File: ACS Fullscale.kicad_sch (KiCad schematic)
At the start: 19 parts, among them J1 Pulse-20, J2 Conn_01x02, U1 SN65HVD230, U11 R-78E5.0-1.0, U2 MS5611-01BA, U3 4001, U4 Teensy4.1, U5 TPS62202DBV, U6 BHI360, U7 TXS0108EPW

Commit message: hi
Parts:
- removed U3: 4001, symbol 4xxx_IEEE:4001
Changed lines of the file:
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@@
-	(wire
-		(pts
-			(xy 72.39 138.43) (xy 120.65 138.43)
-		)
-		(stroke
-			(width 0)
-			(type default)
-		)
-	)
 	(wire
 		(pts
@@
 	(wire
 		(pts
-			(xy 139.7 143.51) (xy 139.7 127)
-		)
-		(stroke
-			(width 0)
-			(type default)
-		)
-	)
-	(wire
-		(pts
 			(xy 38.1 31.75) (xy 38.1 48.26)
 		)
@@
 	(wire
 		(pts
-			(xy 156.21 154.94) (xy 156.21 162.56)
-		)
-		(stroke
-			(width 0)
-			(type default)
-		)
-	)
-	(wire
-		(pts
 			(xy 73.66 109.22) (xy 81.28 109.22)
 		)
@@
 	(wire
 		(pts
-			(xy 163.83 162.56) (xy 156.21 162.56)
-		)
-		(stroke
-			(width 0)
-			(type default)
-		)
-	)
-	(wire
-		(pts
 			(xy 95.25 31.75) (xy 95.25 33.02)
 		)
@@
 		(pts
 			(xy 80.01 165.1) (xy 80.01 167.64)
-		)
-		(stroke
-			(width 0)
-			(type default)
-		)
-	)
-	(wire
-		(pts
-			(xy 127 127) (xy 139.7 127)
 		)
 		(stroke
@@
 					(unit 1)
 				)
-			)
-		)
-	)
-	(symbol
-		(lib_id "4xxx_IEEE:4001")
-		(at 81.28 144.78 0)
-		(unit 1)
-		(exclude_from_sim no)
-		(in_bom yes)
-		(on_board yes)
-		(dnp no)
-		(fields_autoplaced yes)
-		(property "Reference" "U3"
-			(at 90.17 138.3598 0)
-			(effects
-				(font
-					(size 1.27 1.27)
-				)
-			)
-		)
-		(property "Value" "4001"
-			(at 90.17 140.8998 0)
-			(effects
-				(font
-					(size 1.27 1.27)
-				)
-			)
-		)
-		(property "Footprint" ""
-			(at 81.28 144.78 0)
-			(effects
-				(font
-					(size 1.27 1.27)
-				)
-				(hide yes)
-			)
-		)
-		(property "Datasheet" ""
-			(at 81.28 144.78 0)
-			(effects
-				(font
-					(size 1.27 1.27)
-				)
-				(hide yes)
-			)
-		)
-		(property "Description" ""
-			(at 81.28 144.78 0)
-			(effects
-				(font
-					(size 1.27 1.27)
-				)
-				(hide yes)
-			)
-		)
-		(pin "9"
-		)
-		(pin "12"
-		)
-		(pin "10"
-		)
-		(pin "13"
-		)
-		(pin "11"
-		)
-		(pin "8"
-		)
-		(pin "4"
-		)
-		(pin "6"
-		)
-		(pin "5"
-		)
-		(pin "3"
-		)
-		(pin "2"
-		)
-		(pin "1"
-		)
-		(pin "7"
-		)
-		(pin "14"
-		)
-		(instances
-			(project ""
-				(path "/51f244b9-9601-4f29-b08e-b866e02fd2b7"
-					(reference "U3")
-					(unit 1)
-				)

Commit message: fix lib
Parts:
- removed J1: Pulse-20, Sensor_Motion:Pulse-20, symbol Sensor_Motion:Pulse-20
- removed U11: R-78E5.0-1.0, R-78E5.0-1.0:R-78C&slash_E-1.0_SIP3_11.6X8.5X10.4_RCP, symbol R-78E5.0-1.0:R-78E5.0-1.0
- removed U4: Teensy4.1, teensy:Teensy41, symbol teensy:Teensy4.1
- removed U6: BHI360, Sensor_Motion:BHI360 Shuttle Board, symbol Sensor_Motion:BHI360_Shuttle_Board
- added J1: Pulse-20, ACS_Footprint_Library:Pulse-20, symbol ACS_symbol_Library:Pulse-20
- added U11: R-78E5.0-1.0, Converter_DCDC:Converter_DCDC_RECOM_R-78E-0.5_THT, symbol Regulator_Switching:R-78E5.0-1.0
- added U4: Teensy4.1, ACS_Footprint_Library:Teensy41, symbol ACS_symbol_Library:Teensy4.1
- added U6: BHI360, ACS_Footprint_Library:BHI360 Shuttle Board, symbol ACS_symbol_Library:BHI360_Shuttle_Board
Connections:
- net +1V8: now also U6.JP1_1 (VDD), U6.JP1_2 (VDDIO)
- net +3V3: now also U4.15 (3V3), U4.46 (3V3)
- net +5V: now also J1.6 (VIN), U11.3 (OUT), U4.48 (VIN)
- net +BATT: now also U11.1 (IN)
- net BT3: now also U4.26 (34_RX8)
- net CANH: now also J1.5 (CAN_H)
- net CANL: now also J1.10 (CAN_L)
- net CANRX: now also U4.45 (23_A9_CRX1_MCLK1)
- net CANTX: now also U4.44 (22_A8_CTX1)
- net CS0: now also U4.12 (10_CS_MQSR)
- net CS1: now also U4.20 (28_RX7)
- net CS2: now also U4.29 (37_CS)
- net CS3: now also U4.28 (36_CS)
- net CS_1V8: now also U6.JP2_1 (CS)
- net GND: now also J1.1 (GND), U11.2 (GND), U4.1 (GND), U4.34 (GND), U4.47 (GND), U6.JP1_3 (GND)
- net INT0: now also U4.11 (9_OUT1C)
- net INT2: now also U4.32 (40_A16)
- net INT3: now also U4.25 (33_MCLK2)
- net INT_1V8: now also U6.JP1_6 (GPIO2/INT1)
- net MISO0: now also U4.14 (12_MISO_MQSL)
- net MISO1: now also U4.3 (1_TX1_CTX2_MISO1)
- net MISO_1V8: now also U6.JP2_3 (SDO)
- net MOSI0: now also U4.13 (11_MOSI_CTX1)
- net MOSI1: now also U4.18 (26_A12_MOSI1)
- net MOSI_1V8: now also U6.JP2_4 (SDI/SDA)
- net RST2: now also U4.33 (41_A17)
- net RST3: now also U4.27 (35_TX8)
- net RST_1V8: now also U6.JP1_5 (GPIO1)
- net SCK0: now also U4.35 (13_SCK_LED)
- net SCK1: now also U4.19 (27_A13_SCK1)
- net SCK_1V8: now also U6.JP2_2 (SCK/SCL)
- net WAKE3: now also U4.24 (32_OUT1B)
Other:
- moved on the sheet: C2, C3

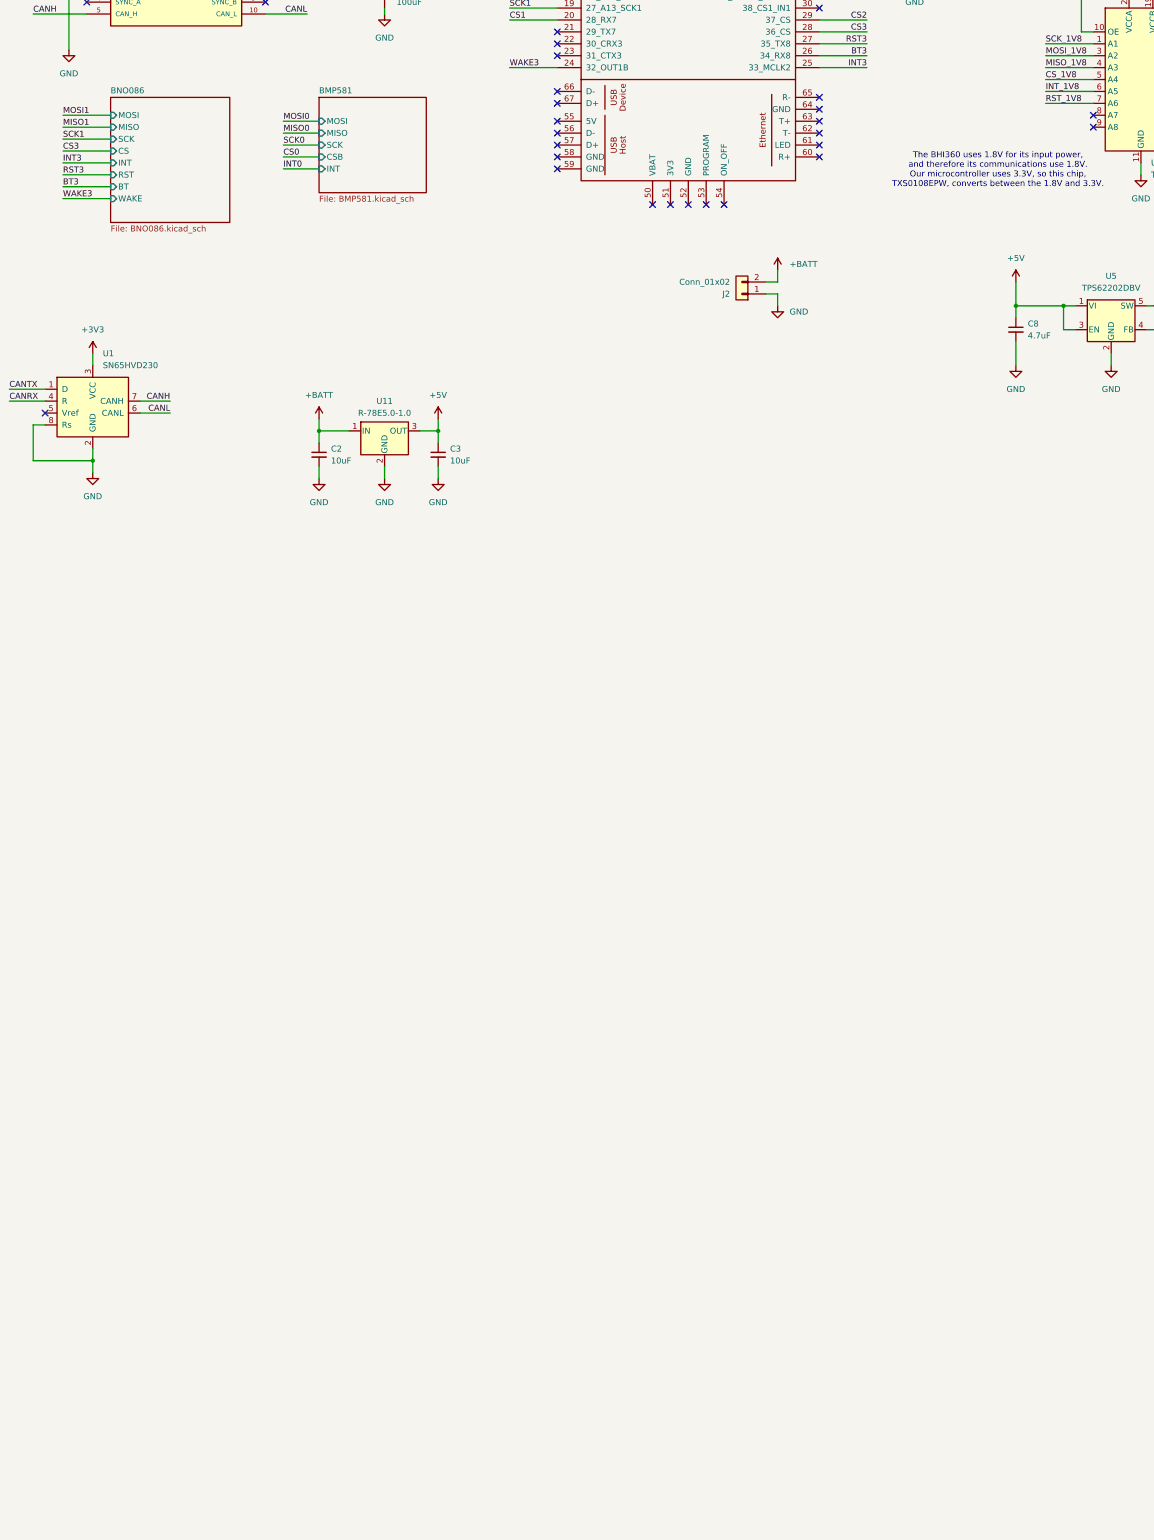
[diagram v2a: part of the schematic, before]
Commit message: I added the symbols for the CM5 in accordance with https://pip.raspberrypi.com/categories/1098-design-files, including all related files.
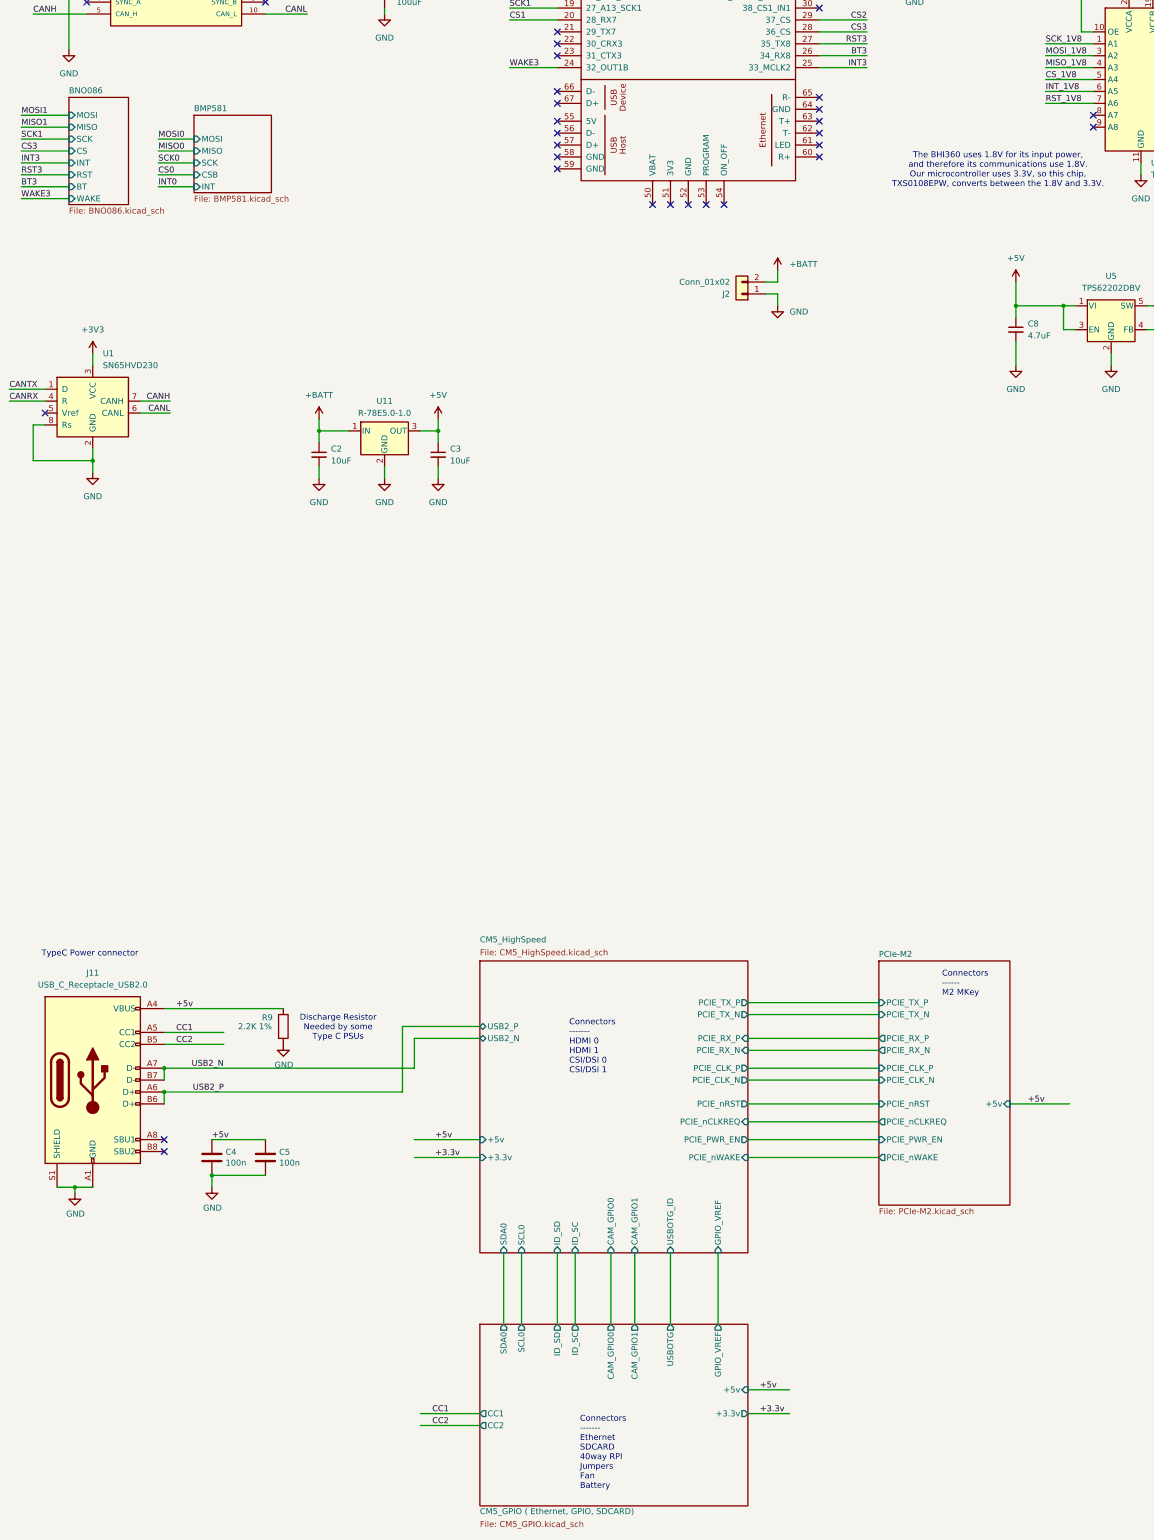
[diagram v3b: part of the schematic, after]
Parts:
- added C4, C5: 100n, Capacitor_SMD:C_0402_1005Metric, symbol Device:C
- added J11: USB_C_Receptacle_USB2.0, Connector_USB:USB_C_Receptacle_GCT_USB4105-xx-A_16P_TopMnt_Horizontal, symbol Connector:USB_C_Receptacle_USB2.0_16P
- added R9: 2.2K 1%, Resistor_SMD:R_0402_1005Metric, symbol Device:R
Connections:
- net GND: now also C4.2, C5.2, J11.A1 (GND), J11.A12 (GND), J11.B1 (GND), J11.B12 (GND), J11.S1 (SHIELD), R9.2
- new net +5v: C4.1, C5.1, J11.A4 (VBUS), J11.A9 (VBUS), J11.B4 (VBUS), J11.B9 (VBUS), R9.1
- new net CC1: J11.A5 (CC1)
- new net CC2: J11.B5 (CC2)
- new net USB2_N: J11.A7 (D-), J11.B7 (D-)
- new net USB2_P: J11.A6 (D+), J11.B6 (D+)
- no-connect marks 54 -> 56
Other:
- added sheet CM5_GPIO ( Ethernet, GPIO, SDCARD) (CM5_GPIO.kicad_sch)
- added sheet CM5_HighSpeed (CM5_HighSpeed.kicad_sch)
- added sheet PCIe-M2 (PCIe-M2.kicad_sch)
- note added: "Connectors ------ M2 MKey"
- note added: "Connectors ------- Ethernet SDCARD 40way RPI Jumpers Fan Battery"
- note added: "Connectors ------- HDMI 0 HDMI 1 CSI/DSI 0 CSI/DSI 1"
- note added: "Discharge Resistor Needed by some Type C PSUs"
- note added: "TypeC Power connector"

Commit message: yes
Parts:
- renumbered J11 to J16, R9 to R21
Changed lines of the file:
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@@
 		(dnp no)
 		(fields_autoplaced yes)
-		(property "Reference" "J11"
+		(property "Reference" "J16"
 			(at 33.02 283.21 0)
 			(effects
@@
 			(project "ACS Fullscale"
 				(path "/51f244b9-9601-4f29-b08e-b866e02fd2b7"
-					(reference "J11")
+					(reference "J16")
 					(unit 1)
 				)
@@
 		(on_board yes)
 		(dnp no)
-		(property "Reference" "R9"
+		(property "Reference" "R21"
 			(at 69.088 292.735 0)
 			(effects
@@
 			(project "ACS Fullscale"
 				(path "/51f244b9-9601-4f29-b08e-b866e02fd2b7"
-					(reference "R9")
-					(unit 1)
-				)
+					(reference "R21")
+					(unit 1)
+				)

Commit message: A lot of stuff
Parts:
- removed C4, C5: 100n, Capacitor_SMD:C_0402_1005Metric, symbol Device:C
- removed J16: USB_C_Receptacle_USB2.0, Connector_USB:USB_C_Receptacle_GCT_USB4105-xx-A_16P_TopMnt_Horizontal, symbol Connector:USB_C_Receptacle_USB2.0_16P
- removed R21: 2.2K 1%, Resistor_SMD:R_0402_1005Metric, symbol Device:R
- added BUZZ1: CD-1206-SMT, ACS_Footprint_Library:CUI_CD-1206-SMT, symbol ACS_symbol_Library:CD-1206-SMT
- added D3: D, Diode_SMD:D_SOD-323, symbol Device:D
- added Q1: Q_NPN_BEC, Package_TO_SOT_SMD:TSOT-23, symbol Transistor_BJT:Q_NPN_BEC
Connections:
- net +5V: now also BUZZ1.P, D3.1 (K)
- net BT3: now also U4.20 (28_RX7); no longer U4.26 (34_RX8)
- net CS0: now also U4.11 (9_OUT1C); no longer U4.12 (10_CS_MQSR)
- net CS1: now also U4.32 (40_A16); no longer U4.20 (28_RX7)
- net CS2: now also U4.33 (41_A17); no longer U4.29 (37_CS)
- net CS3: now also U4.24 (32_OUT1B); no longer U4.28 (36_CS)
- net GND: now also Q1.2 (E)
- net INT0: now also U4.8 (6_OUT1D); no longer U4.11 (9_OUT1C)
- net INT2: now also U4.16 (24_A10_TX6_SCL2); no longer U4.32 (40_A16)
- net INT3: now also U4.23 (31_CTX3); no longer U4.25 (33_MCLK2)
- net RST2: now also U4.17 (25_A11_RX6_SDA2); no longer U4.33 (41_A17)
- net RST3: now also U4.22 (30_CRX3); no longer U4.27 (35_TX8)
- net WAKE3: now also U4.21 (29_TX7); no longer U4.24 (32_OUT1B)
- net TX2: now reaches U4.10 (8_TX2_IN1)
- net Buzz: now reaches U4.39 (17_A3_TX4_SDA1)
- net Buzz: now also Q1.1 (B)
- net RX2: now reaches U4.9 (7_RX2_OUT1A)
- new net: BUZZ1.M, D3.2 (A), Q1.3 (C)
- no-connect marks 56 -> 45
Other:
- removed sheet PCIe-M2
- sheet CM5_GPIO ( Ethernet, GPIO, SDCARD) ports: added RX, TX; removed none
- note removed: "Connectors ------ M2 MKey"
- note removed: "Discharge Resistor Needed by some Type C PSUs"
- note removed: "TypeC Power connector"

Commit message: ryan
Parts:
- added J4, J5: Conn_01x03, Connector_PinHeader_2.54mm:PinHeader_1x03_P2.54mm_Vertical, symbol Connector_Generic:Conn_01x03
- added R2, R3: 120, LED_SMD:LED_0603_1608Metric, symbol Device:R_Small_US
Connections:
- net +BATT: now also J4.2 (Pin_2), J5.2 (Pin_2)
- net CANH: now also R2.1, R3.1
- net CANL: now also R2.2, R3.2
- net GND: now also J4.3 (Pin_3), J5.3 (Pin_3)
- net PWM2: now reaches U4.28 (36_CS)
- net PWM1: now reaches U4.29 (37_CS)
- net Motor1: now reaches U4.40 (18_A4_SDA)
- net Motor1: now also J4.1 (Pin_1)
- net Motor2: now reaches U4.41 (19_A5_SCL)
- net Motor2: now also J5.1 (Pin_1)
- no-connect marks 45 -> 46
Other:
- sheet CM5_GPIO ( Ethernet, GPIO, SDCARD) ports: added GPIO12, GPIO13; removed none
- title: (none) -> Apogee Control System PCB
- moved on the sheet: BUZZ1, C2, C3, D3, Q1, U1, U11

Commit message: lots
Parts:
- removed C19, C21: 100uF, Capacitor_THT:CP_Radial_D6.3mm_P2.50mm, symbol Device:C_Small
- removed C8: 4.7uF, Capacitor_SMD:C_0603_1608Metric, symbol Device:C_Small
- removed C9: 10uF, Capacitor_SMD:C_0603_1608Metric, symbol Device:C_Small
- removed L2: 10uH, Inductor_SMD:L_0603_1608Metric, symbol Device:L_Small
- removed R2, R3: 120, LED_SMD:LED_0603_1608Metric, symbol Device:R_Small_US
- removed U1: SN65HVD230, Package_SO:SOIC-8_3.9x4.9mm_P1.27mm, symbol Interface_CAN_LIN:SN65HVD230
- removed U2: MS5611-01BA, Package_LGA:LGA-8_3x5mm_P1.25mm, symbol Sensor_Pressure:MS5611-01BA
- removed U5: TPS62202DBV, Package_TO_SOT_SMD:SOT-23-5, symbol Regulator_Switching:TPS62202DBV
- removed U6: BHI360, ACS_Footprint_Library:BHI360 Shuttle Board, symbol ACS_symbol_Library:BHI360_Shuttle_Board
- removed U7: TXS0108EPW, Package_SO:TSSOP-20_4.4x6.5mm_P0.65mm, symbol Logic_LevelTranslator:TXS0108EPW
- added C4: 100uF, Capacitor_SMD:C_1206_3216Metric, symbol Device:C_Small
- added JP1: BNO_DI, Jumper:SolderJumper-3_P1.3mm_Bridged2Bar12_RoundedPad1.0x1.5mm, symbol Jumper:SolderJumper_3_Bridged12
- added JP10: LSM_SDOAG, Jumper:SolderJumper-3_P1.3mm_Bridged2Bar12_RoundedPad1.0x1.5mm, symbol Jumper:SolderJumper_3_Bridged12
- added JP11: LSM_SDOM, Jumper:SolderJumper-3_P1.3mm_Bridged2Bar12_RoundedPad1.0x1.5mm, symbol Jumper:SolderJumper_3_Bridged12
- added JP12: BNO_MOSI, Jumper:SolderJumper-3_P1.3mm_Bridged2Bar12_RoundedPad1.0x1.5mm, symbol Jumper:SolderJumper_3_Bridged12
- added JP13: BNO_SCK, Jumper:SolderJumper-3_P1.3mm_Bridged2Bar12_RoundedPad1.0x1.5mm, symbol Jumper:SolderJumper_3_Bridged12
- added JP14: BNO_MISO, Jumper:SolderJumper-3_P1.3mm_Bridged2Bar12_RoundedPad1.0x1.5mm, symbol Jumper:SolderJumper_3_Bridged12
- added JP15, JP8: LSM_SCK, Jumper:SolderJumper-3_P1.3mm_Bridged2Bar12_RoundedPad1.0x1.5mm, symbol Jumper:SolderJumper_3_Bridged12
- added JP16, JP9: LSM_MOSI, Jumper:SolderJumper-3_P1.3mm_Bridged2Bar12_RoundedPad1.0x1.5mm, symbol Jumper:SolderJumper_3_Bridged12
- added JP17, JP19: LSMAG_MISO, Jumper:SolderJumper-3_P1.3mm_Bridged2Bar12_RoundedPad1.0x1.5mm, symbol Jumper:SolderJumper_3_Bridged12
- added JP18: ICM_SCL, Jumper:SolderJumper-3_P1.3mm_Bridged2Bar12_RoundedPad1.0x1.5mm, symbol Jumper:SolderJumper_3_Bridged12
- added JP2: BNO_SCL, Jumper:SolderJumper-3_P1.3mm_Bridged2Bar12_RoundedPad1.0x1.5mm, symbol Jumper:SolderJumper_3_Bridged12
- added JP20: LSMM_MISO, Jumper:SolderJumper-3_P1.3mm_Bridged2Bar12_RoundedPad1.0x1.5mm, symbol Jumper:SolderJumper_3_Bridged12
- added JP21: ICM_SDA, Jumper:SolderJumper-3_P1.3mm_Bridged2Bar12_RoundedPad1.0x1.5mm, symbol Jumper:SolderJumper_3_Bridged12
- added JP22: ICM_SDO, Jumper:SolderJumper-3_P1.3mm_Bridged2Bar12_RoundedPad1.0x1.5mm, symbol Jumper:SolderJumper_3_Bridged12
- added JP3: BNO_SDA, Jumper:SolderJumper-3_P1.3mm_Bridged2Bar12_RoundedPad1.0x1.5mm, symbol Jumper:SolderJumper_3_Bridged12
- added JP4: BNO_P0, Jumper:SolderJumper-3_P1.3mm_Bridged2Bar12_RoundedPad1.0x1.5mm, symbol Jumper:SolderJumper_3_Bridged12
- added JP5: BNO_P1, Jumper:SolderJumper-3_P1.3mm_Bridged2Bar12_RoundedPad1.0x1.5mm, symbol Jumper:SolderJumper_3_Bridged12
- added JP6: LSM_SCL, Jumper:SolderJumper-3_P1.3mm_Bridged2Bar12_RoundedPad1.0x1.5mm, symbol Jumper:SolderJumper_3_Bridged12
- added JP7: LSM_SDA, Jumper:SolderJumper-3_P1.3mm_Bridged2Bar12_RoundedPad1.0x1.5mm, symbol Jumper:SolderJumper_3_Bridged12
- added R1: 10k, Resistor_SMD:R_0805_2012Metric_Pad1.20x1.40mm_HandSolder, symbol Device:R_Small_US
- added U2: MS5611-01BA03, Sensor_Pressure:HiLetgo MS5611, symbol Sensor_Pressure:HiLetgo_MS5611-01BA03
- added U3: Adafruit_BNO086, Sensor_Motion:Adafruit BNO086, symbol Sensor_Motion:Adafruit_BNO086
- added U6: ICM20948, Sensor_Motion:Adafruit ICM20948, symbol Sensor_Motion:Adafruit_ICM20948
- added U7: LSM9DS1, Sensor_Motion:Adafruit LSM9DS1, symbol Sensor_Motion:Adafruit_LSM9DS1
- added U9: LTC2851xS8, Package_SO:SOIC-8_3.9x4.9mm_P1.27mm, symbol Interface_UART:LTC2851xS8
- C1: value 100nF -> 100uF; footprint Capacitor_SMD:C_0603_1608Metric -> Capacitor_SMD:C_1206_3216Metric
- C20: footprint Capacitor_THT:CP_Radial_D6.3mm_P2.50mm -> Capacitor_SMD:C_1206_3216Metric
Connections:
- net CANRX is gone; now on net PWM1: U4.45 (23_A9_CRX1_MCLK1)
- net CANTX is gone; now on net PWM2: U4.44 (22_A8_CTX1)
- net +3V3: now also JP5.1 (A), R1.2, U2.1 (VCC), U3.1 (VIN), U6.1 (VIN), U7.1 (VIN), U9.1 (VCC)
- net +BATT: now also C4.1
- net Buzz: no longer U4.39 (17_A3_TX4_SDA1)
- net GND: now also C4.2, JP4.3 (B), JP5.3 (B), U2.2 (GND), U2.7 (PS), U3.3 (GND), U6.10 (GND), U6.3 (GND), U7.3 (GND), U9.4 (GND)
- net MISO0: now also JP14.1 (A), JP17.3 (B), JP19.3 (B), JP20.3 (B)
- net MISO1: now also JP14.3 (B), JP17.1 (A), JP19.1 (A), JP20.1 (A), U2.6 (SDO)
- net MOSI0: now also JP12.1 (A), JP16.3 (B), JP9.3 (B)
- net MOSI1: now also JP12.3 (B), JP16.1 (A), JP9.1 (A), U2.4 (SDA)
- net Motor1: no longer U4.40 (18_A4_SDA)
- net Motor2: no longer U4.41 (19_A5_SCL)
- net PWM1: no longer U4.29 (37_CS)
- net PWM2: no longer U4.28 (36_CS)
- net SCK0: now also JP13.1 (A), JP15.3 (B), JP8.3 (B)
- net SCK1: now also JP13.3 (B), JP15.1 (A), JP8.1 (A), U2.3 (SCL)
- net BMP_INT: now reaches U4.25 (33_MCLK2)
- net BMP_CS: now reaches U4.27 (35_TX8)
- net LSM_INTM: now reaches U4.31 (39_MISO1_OUT1A)
- net LSM_INTM: now also U7.13 (INTM)
- net LSM_CSM: now reaches U4.36 (14_A0_TX3_SPDIF_OUT)
- net LSM_CSM: now also U7.7 (CSM)
- net LSM_CSAG: now reaches U4.37 (15_A1_RX3_SPDIF_IN)
- net LSM_CSAG: now also U7.6 (CSAG)
- net BNO_INT: now reaches U4.4 (2_OUT2)
- net BNO_INT: now also U3.6 (~{INT})
- net CS_MS: now reaches U4.43 (21_A7_RX5_BCLK1)
- net CS_MS: now also U2.5 (CSB)
- net BNO_RST: now reaches U4.5 (3_LRCLK2)
- net BNO_RST: now also U3.10 (~{RST})
- net BNO_CS: now reaches U4.6 (4_BCLK2)
- net BNO_CS: now also U3.12 (CS)
- net Rx+: now reaches J1.2 (PORT_A_Rx+)
- net Rx+: now also U9.6 (Z)
- net Tx+: now reaches J1.3 (PORT_A_Tx+)
- net Tx+: now also U9.8 (A)
- net RX-: now reaches J1.7 (PORT_A_RX-)
- net RX-: now also U9.5 (Y)
- net TX-: now reaches J1.8 (PORT_A_TX-)
- net TX-: now also U9.7 (B)
- net BT3 renamed RX7
- net RX7: now also U9.2 (RO)
- net CANH: no longer names the net of J1.5 (CAN_H)
- net CANL: no longer names the net of J1.10 (CAN_L)
- net CS0: no longer names the net of U4.11 (9_OUT1C)
- net CS1 renamed LSM_INT1
- net LSM_INT1: now also U7.12 (INT1)
- net CS2 renamed LSM_INT2
- net LSM_INT2: now also U7.11 (INT2)
- net CS3: no longer names the net of U4.24 (32_OUT1B)
- net INT0: no longer names the net of U4.8 (6_OUT1D)
- net INT2 renamed ICM_INT
- net ICM_INT: now also U6.6 (INT)
- net INT3: no longer names the net of U4.23 (31_CTX3)
- net RST2 renamed ICM_CS
- net ICM_CS: now also U6.12 (CS)
- net RST3: no longer names the net of U4.22 (30_CRX3)
- net WAKE3 renamed TX7
- net TX7: now also U9.3 (DI)
- new net: JP16.2 (C), JP7.1 (A)
- new net: JP10.1 (A), JP19.2 (C)
- new net: JP21.1 (A), JP9.2 (C)
- new net: JP11.1 (A), JP20.2 (C)
- new net: JP1.1 (A), JP12.2 (C)
- new net: JP13.2 (C), JP2.1 (A)
- new net: JP15.2 (C), JP6.1 (A)
- new net: JP17.2 (C), JP22.1 (A)
- new net: JP14.2 (C), JP3.1 (A)
- new net: JP18.1 (A), JP8.2 (C)
- new net BNO_DI: JP1.2 (C), U3.11 (DI)
- new net BNO_P0: JP4.2 (C), U3.8 (P0)
- new net BNO_P1: JP5.2 (C), U3.9 (P1)
- new net BNO_SCL: JP2.2 (C), U3.4 (SCL)
- new net BNO_SDA: JP3.2 (C), U3.5 (SDA)
- new net BNO_WAKE: JP4.1 (A), R1.1
- new net ICM_SCL: JP18.2 (C), U6.4 (SCL)
- new net ICM_SDA: JP21.2 (C), U6.5 (SDA)
- new net ICM_SDO: JP22.2 (C), U6.11 (SDO)
- new net LSM_SCL: JP6.2 (C), U7.4 (SCL)
- new net LSM_SDA: JP7.2 (C), U7.5 (SDA)
- new net LSM_SDOAG: JP10.2 (C), U7.8 (SDOAG)
- new net LSM_SDOM: JP11.2 (C), U7.9 (SDOM)
- new net SCL: JP18.3 (B), JP2.3 (B), JP6.3 (B), U4.41 (19_A5_SCL)
- new net SDA: JP21.3 (B), JP3.3 (B), JP7.3 (B), U4.40 (18_A4_SDA)
- no-connect marks 46 -> 39
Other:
- removed sheet CM5_GPIO ( Ethernet, GPIO, SDCARD)
- removed sheet CM5_HighSpeed
- sheet BNO086 ports: added none; removed BT
- note removed: "Connectors ------- Ethernet SDCARD 40way RPI Jumpers Fan Battery"
- note removed: "Connectors ------- HDMI 0 HDMI 1 CSI/DSI 0 CSI/DSI 1"
- note removed: "The BHI360 uses 1.8V for its input power, and therefore its communications use 1.8V. Our microcontroller uses 3.3V, so this chip, TXS0108EPW, converts between the 1.8V and 3.3V."
- moved on the sheet: J1
